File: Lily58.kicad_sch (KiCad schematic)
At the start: 41 parts, among them J1 USB_C_Receptacle, J2 USB_C_Receptacle, J3 Conn_01x03_Pin, SW1 SW_SPST, U1 BQ24091DGQ, U2 TPS63000, U3 TPS63000

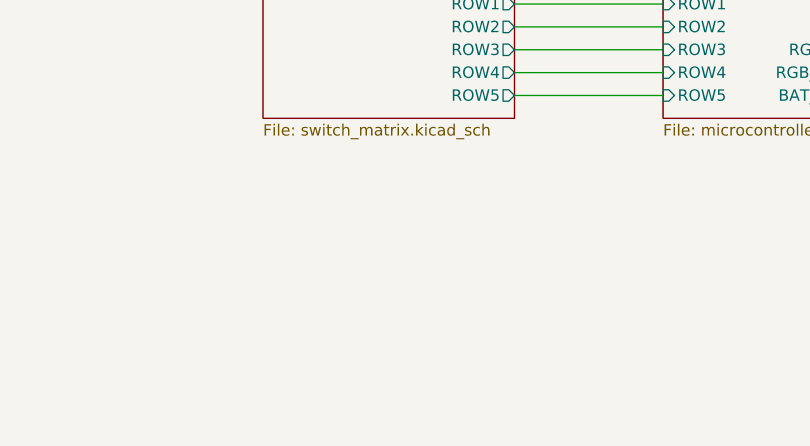
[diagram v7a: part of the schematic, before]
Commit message: added rgb matrix sheet
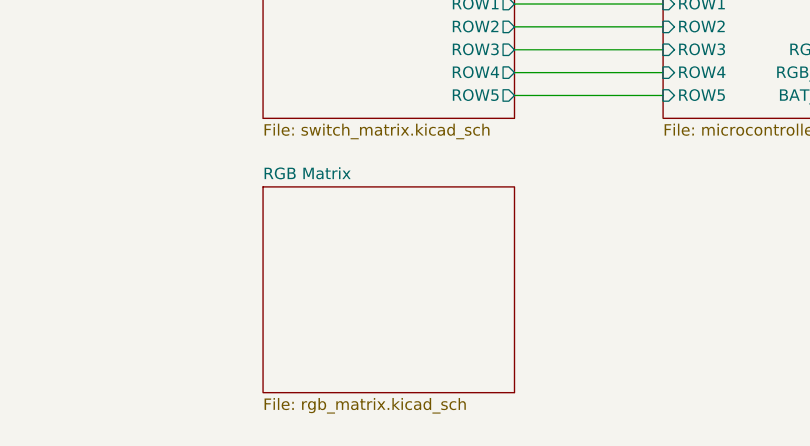
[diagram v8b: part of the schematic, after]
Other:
- added sheet RGB Matrix (rgb_matrix.kicad_sch)
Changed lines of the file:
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@@
+    )
+  )
+  (sheet (at 74.93 163.83) (size 27.94 22.86) (fields_autoplaced)
+    (stroke (width 0.1524) (type solid))
+    (fill (color 0 0 0 0.0000))
+    (property "Sheetname" "RGB Matrix" (at 74.93 163.1184 0)
+      (effects (font (size 1.27 1.27)) (justify left bottom))
+    )
+    (property "Sheetfile" "rgb_matrix.kicad_sch" (at 74.93 187.2746 0)
+      (effects (font (size 1.27 1.27)) (justify left top))
+    )
+    (instances
+      (project "Lily58"
+        (path "/a0958e12-2248-4ac3-b259-3086ac296b70" (page "4"))
+      )
     )
   )
